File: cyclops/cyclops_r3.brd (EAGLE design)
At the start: 124.5 x 79.9 mm, 138 parts, among them Q1 BC817, Q2 IRF510, U1 MCP4921, U10 TLV2374, U11 THS4281, U12 MAX4564, U13 ZXTD, U14 ZXTD, U2 ADG3301, U3 MCP4022-50k, U4 LT1931, U5 LT1963A, U6 337L, U7 TLV3701, U8 ADR03, U9 OP1177, X1 SLP3, X2 SLP3, X3 SLP3

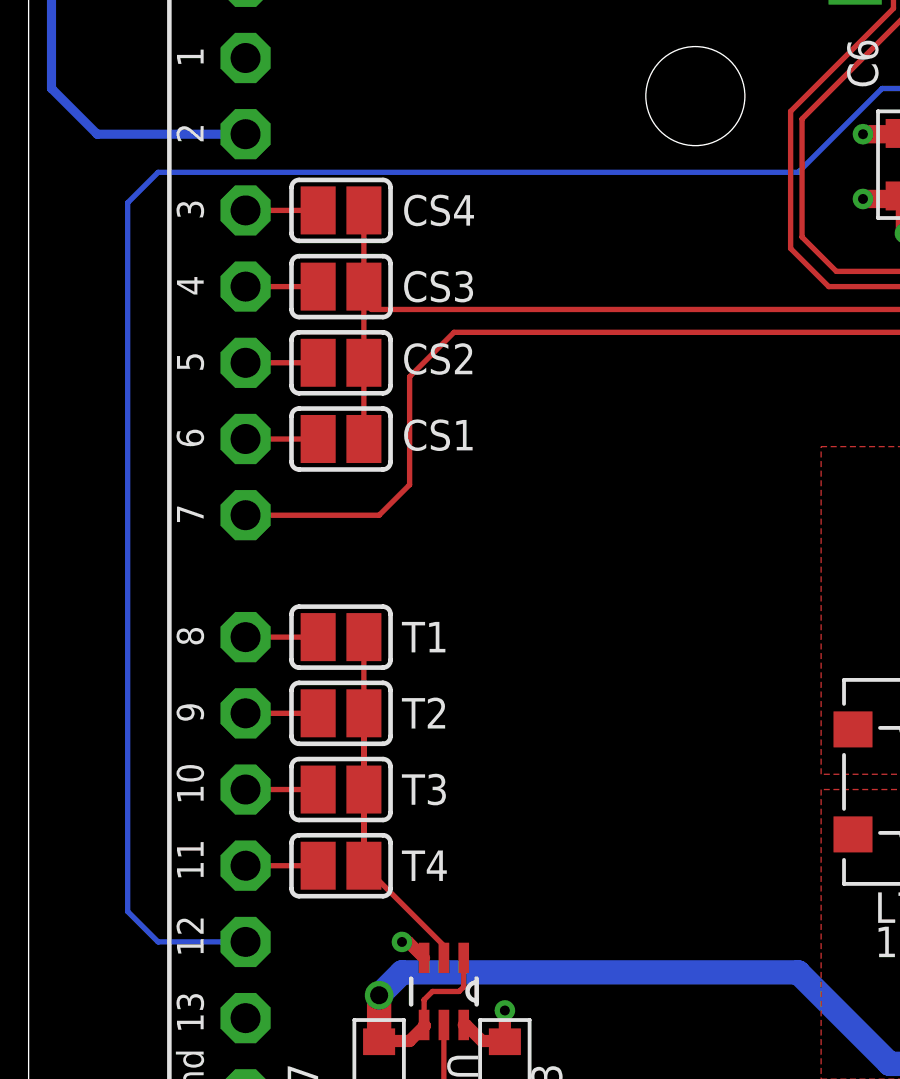
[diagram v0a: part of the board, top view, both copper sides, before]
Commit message: Refixed the incorrect labels on the jumper pads.
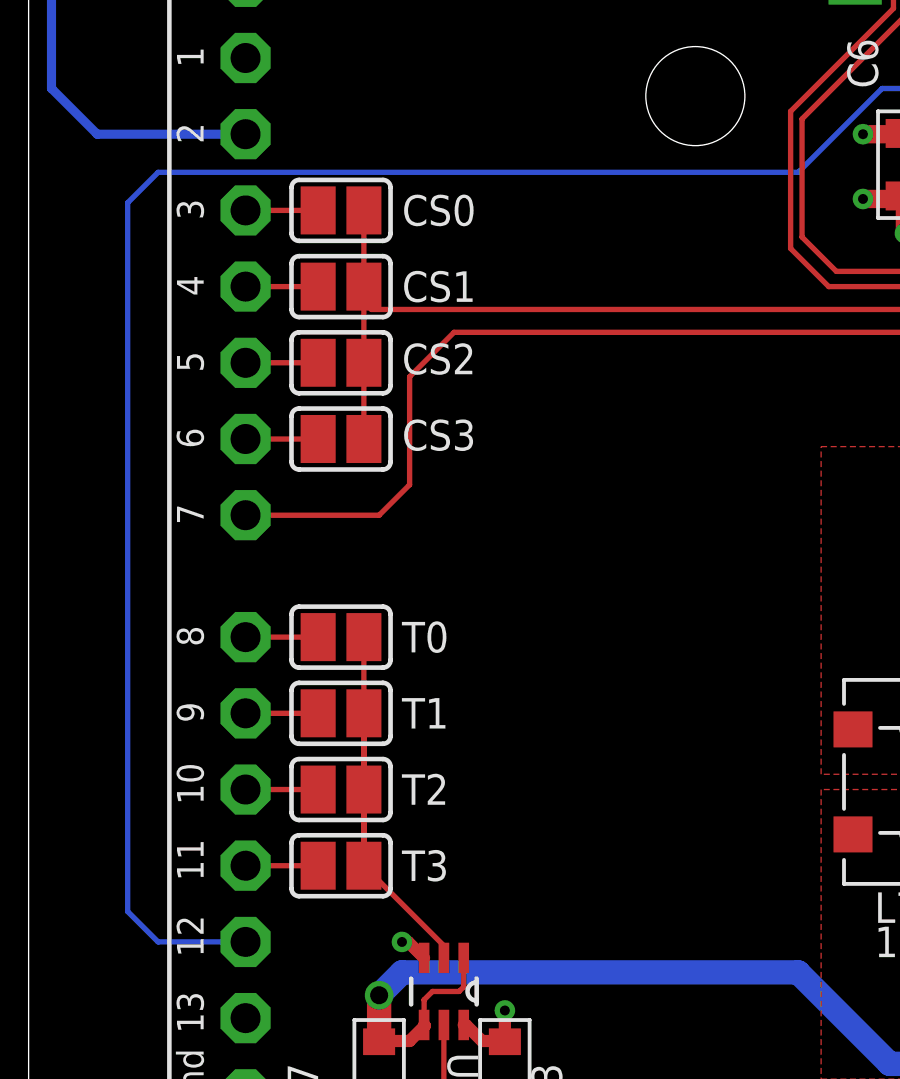
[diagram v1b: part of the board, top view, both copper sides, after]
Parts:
- removed T4: (no value), cyclops:SJ
- added T0: (no value), cyclops:SJ
- moved CS1 5.08 mm to (10.4, 53.3)
- moved CS3 5.08 mm to (10.4, 48.3)
- moved T1 2.54 mm to (10.4, 39.1)
- moved T2 2.54 mm to (10.4, 36.6)
- moved T3 2.54 mm to (10.4, 34.0)
- renumbered CS4 to CS0
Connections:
- net CS1: now also CS1.1; no longer CS3.1
- net CS3: now also CS3.1; no longer CS1.1
- net T0: now also T0.2; no longer T1.2
- net T1: now also T1.2; no longer T2.2
- net T2: now also T2.2; no longer T3.2
- net T3: now also T3.2; no longer T4.2
- net TRIG: now also T0.1; no longer T4.1
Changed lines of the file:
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@@
 <attribute name="VALUE" x="76.835" y="46.355" size="1.016" layer="27" font="vector" ratio="18" rot="R90" align="center-left"/>
 </element>
-<element name="CS1" library="cyclops" package="SJ" value="" x="10.414" y="48.26" smashed="yes">
+<element name="CS3" library="cyclops" package="SJ" value="" x="10.414" y="48.26" smashed="yes">
 <attribute name="NAME" x="12.446" y="47.879" size="1.016" layer="25" font="vector" ratio="18"/>
 <attribute name="VALUE" x="10.8141" y="48.26" size="0.02" layer="27"/>
@@
 <attribute name="VALUE" x="10.8141" y="50.8" size="0.02" layer="27"/>
 </element>
-<element name="CS3" library="cyclops" package="SJ" value="" x="10.414" y="53.34" smashed="yes">
+<element name="CS1" library="cyclops" package="SJ" value="" x="10.414" y="53.34" smashed="yes">
 <attribute name="NAME" x="12.446" y="52.832" size="1.016" layer="25" font="vector" ratio="18"/>
 <attribute name="VALUE" x="10.8141" y="53.34" size="0.02" layer="27"/>
 </element>
-<element name="CS4" library="cyclops" package="SJ" value="" x="10.414" y="55.88" smashed="yes">
+<element name="CS0" library="cyclops" package="SJ" value="" x="10.414" y="55.88" smashed="yes">
 <attribute name="NAME" x="12.446" y="55.372" size="1.016" layer="25" font="vector" ratio="18"/>
 <attribute name="VALUE" x="10.8141" y="55.88" size="0.02" layer="27"/>
@@
 <attribute name="VALUE" x="26.162" y="11.938" size="1.016" layer="27" font="vector" ratio="18" align="center-left"/>
 </element>
-<element name="T1" library="cyclops" package="SJ" value="" x="10.414" y="41.656" smashed="yes" rot="R180">
+<element name="T0" library="cyclops" package="SJ" value="" x="10.414" y="41.656" smashed="yes" rot="R180">
 <attribute name="NAME" x="12.446" y="41.148" size="1.016" layer="25" font="vector" ratio="18"/>
 <attribute name="VALUE" x="10.0139" y="41.656" size="0.02" layer="27" rot="R180"/>
 </element>
-<element name="T2" library="cyclops" package="SJ" value="" x="10.414" y="39.116" smashed="yes" rot="R180">
+<element name="T1" library="cyclops" package="SJ" value="" x="10.414" y="39.116" smashed="yes" rot="R180">
 <attribute name="NAME" x="12.446" y="38.608" size="1.016" layer="25" font="vector" ratio="18"/>
 <attribute name="VALUE" x="10.0139" y="39.116" size="0.02" layer="27" rot="R180"/>
 </element>
-<element name="T3" library="cyclops" package="SJ" value="" x="10.414" y="36.576" smashed="yes" rot="R180">
+<element name="T2" library="cyclops" package="SJ" value="" x="10.414" y="36.576" smashed="yes" rot="R180">
 <attribute name="NAME" x="12.446" y="36.068" size="1.016" layer="25" font="vector" ratio="18"/>
 <attribute name="VALUE" x="10.0139" y="36.576" size="0.02" layer="27" rot="R180"/>
 </element>
-<element name="T4" library="cyclops" package="SJ" value="" x="10.414" y="34.036" smashed="yes" rot="R180">
+<element name="T3" library="cyclops" package="SJ" value="" x="10.414" y="34.036" smashed="yes" rot="R180">
 <attribute name="NAME" x="12.446" y="33.528" size="1.016" layer="25" font="vector" ratio="18"/>
 <attribute name="VALUE" x="10.0139" y="34.036" size="0.02" layer="27" rot="R180"/>
@@
 </signal>
 <signal name="CS0">
-<contactref element="CS4" pad="1"/>
+<contactref element="CS0" pad="1"/>
 <contactref element="LEONARDO" pad="D3"/>
 <wire x1="9.652" y1="55.88" x2="7.232" y2="55.88" width="0.1778" layer="1"/>
 </signal>
 <signal name="CS1">
-<contactref element="CS3" pad="1"/>
+<contactref element="CS1" pad="1"/>
 <contactref element="LEONARDO" pad="D4"/>
 <wire x1="7.232" y1="53.34" x2="9.652" y2="53.34" width="0.1778" layer="1"/>
 </signal>
 <signal name="CS3">
-<contactref element="CS1" pad="1"/>
+<contactref element="CS3" pad="1"/>
 <contactref element="LEONARDO" pad="D6"/>
 <wire x1="7.232" y1="48.26" x2="9.652" y2="48.26" width="0.1778" layer="1"/>
@@
 <signal name="CS">
 <contactref element="U1" pad="2"/>
-<contactref element="CS4" pad="2"/>
+<contactref element="CS0" pad="2"/>
+<contactref element="CS1" pad="2"/>
+<contactref element="CS2" pad="2"/>
 <contactref element="CS3" pad="2"/>
-<contactref element="CS2" pad="2"/>
-<contactref element="CS1" pad="2"/>
 <wire x1="11.176" y1="55.88" x2="11.176" y2="53.34" width="0.1778" layer="1"/>
 <wire x1="11.176" y1="52.832" x2="11.176" y2="53.34" width="0.1778" layer="1"/>
@@
 </signal>
 <signal name="TRIG">
+<contactref element="T0" pad="1"/>
 <contactref element="T1" pad="1"/>
 <contactref element="T2" pad="1"/>
 <contactref element="T3" pad="1"/>
-<contactref element="T4" pad="1"/>
 <wire x1="11.176" y1="34.036" x2="11.176" y2="39.116" width="0.1778" layer="1"/>
 <wire x1="11.176" y1="39.116" x2="11.176" y2="36.576" width="0.1778" layer="1"/>
@@
 </signal>
 <signal name="T0">
-<contactref element="T1" pad="2"/>
+<contactref element="T0" pad="2"/>
 <contactref element="LEONARDO" pad="D8"/>
 <wire x1="9.652" y1="41.656" x2="7.232" y2="41.656" width="0.1778" layer="1"/>
 </signal>
 <signal name="T1">
-<contactref element="T2" pad="2"/>
+<contactref element="T1" pad="2"/>
 <contactref element="LEONARDO" pad="D9"/>
 <wire x1="7.232" y1="39.116" x2="9.652" y2="39.116" width="0.1778" layer="1"/>
 </signal>
 <signal name="T2">
-<contactref element="T3" pad="2"/>
+<contactref element="T2" pad="2"/>
 <contactref element="LEONARDO" pad="D10"/>
 <wire x1="9.652" y1="36.576" x2="7.232" y2="36.576" width="0.1778" layer="1"/>
 </signal>
 <signal name="T3">
-<contactref element="T4" pad="2"/>
+<contactref element="T3" pad="2"/>
 <contactref element="LEONARDO" pad="D11"/>
 <wire x1="7.232" y1="34.036" x2="9.652" y2="34.036" width="0.1778" layer="1"/>

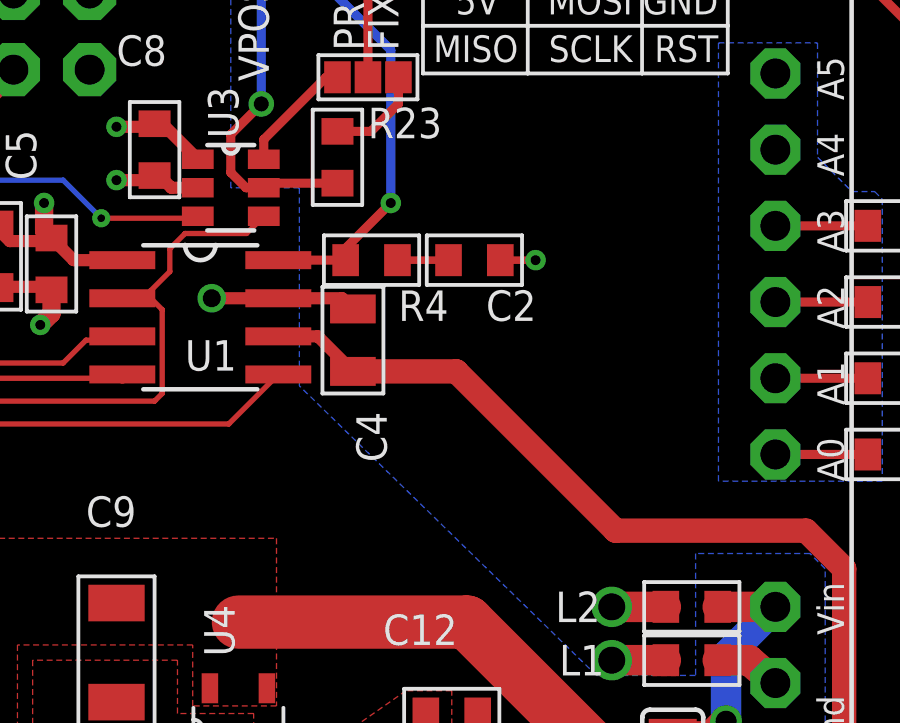
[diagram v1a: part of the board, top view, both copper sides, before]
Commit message: BOM simplification.
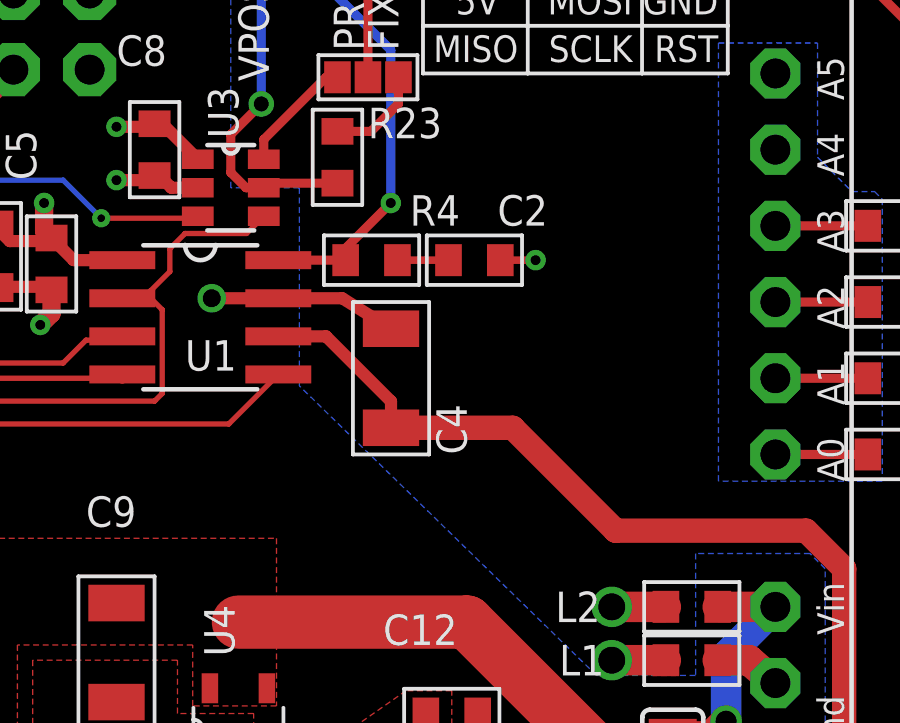
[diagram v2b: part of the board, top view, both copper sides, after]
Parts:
- C4: device cyclops:0805 -> cyclops:1206
- moved C4 1.80 mm to (42.7, 53.3)
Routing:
- net GND: track 116.4 -> 117.8 mm
- net REF2.5: track 65.9 -> 66.4 mm
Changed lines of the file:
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@@
 <attribute name="VALUE" x="33.401" y="51.435" size="1.016" layer="27" font="vector" ratio="18"/>
 </element>
-<element name="C4" library="cyclops" package="0805" value="10uF" x="41.409" y="54.61" smashed="yes" rot="R90">
-<attribute name="MN" value="TDK Corp." x="41.409" y="54.61" size="1.778" layer="27" rot="R90" display="off"/>
-<attribute name="PARTNO" value="C2012X5R1Cxxxxxxx" x="41.409" y="54.61" size="1.778" layer="27" rot="R90" display="off"/>
-<attribute name="DK" value="" x="41.409" y="54.61" size="1.778" layer="27" rot="R90" display="off"/>
-<attribute name="VID" value="DK" x="41.409" y="54.61" size="1.778" layer="27" rot="R90" display="off"/>
-<attribute name="NAME" x="42.538" y="50.546" size="1.016" layer="25" font="vector" ratio="18" rot="R90"/>
-<attribute name="VALUE" x="43.681" y="50.546" size="1.016" layer="27" font="vector" ratio="18" rot="R90"/>
+<element name="C4" library="cyclops" package="1206" value="10uF" x="42.679" y="53.34" smashed="yes" rot="R90">
+<attribute name="NAME" x="45.205" y="50.8" size="1.016" layer="25" font="vector" ratio="18" rot="R90"/>
+<attribute name="VALUE" x="46.602" y="50.8" size="1.016" layer="27" font="vector" ratio="18" rot="R90"/>
 </element>
 <element name="C5" library="cyclops" package="0603" value=".1uF" x="31.362" y="57.15" smashed="yes" rot="R270">
@@
 </element>
 <element name="C2" library="cyclops" package="0603" value="" x="45.459" y="57.277" smashed="yes">
-<attribute name="NAME" x="45.847" y="55.252" size="1.016" layer="25" font="vector" ratio="18"/>
+<attribute name="NAME" x="46.228" y="58.427" size="1.016" layer="25" font="vector" ratio="18"/>
 </element>
 <element name="R4" library="cyclops" package="0603" value="" x="42.03" y="57.277" smashed="yes" rot="R180">
@@
 <attribute name="DK" value="PxxxxHTR-ND" x="42.03" y="57.277" size="1.778" layer="27" rot="R180" display="off"/>
 <attribute name="MPN" value="ERJ-3EKFxxxxV" x="42.03" y="57.277" size="1.778" layer="27" rot="R180" display="off"/>
-<attribute name="NAME" x="42.926" y="55.252" size="1.016" layer="25" font="vector" ratio="18"/>
+<attribute name="NAME" x="43.307" y="58.427" size="1.016" layer="25" font="vector" ratio="18"/>
 </element>
 <element name="R29" library="cyclops" package="0603" value="0" x="78.225" y="38.735" smashed="yes" rot="R180">
@@
 <wire x1="64.636" y1="26.67" x2="64.636" y2="24.518" width="0.3048" layer="1"/>
 <wire x1="64.636" y1="24.518" x2="64.643" y2="24.511" width="0.3048" layer="1"/>
-<wire x1="41.409" y1="53.5686" x2="40.2406" y2="54.737" width="0.4064" layer="1"/>
-<wire x1="40.2406" y1="54.737" x2="38.922" y2="54.737" width="0.4064" layer="1"/>
-<wire x1="41.409" y1="53.5686" x2="44.8564" y2="53.5686" width="0.8128" layer="1"/>
-<wire x1="44.8564" y1="53.5686" x2="50.165" y2="48.26" width="0.8128" layer="1"/>
 <wire x1="50.165" y1="48.26" x2="56.515" y2="48.26" width="0.8128" layer="1"/>
 <wire x1="56.515" y1="48.26" x2="57.785" y2="46.99" width="0.8128" layer="1"/>
@@
 <wire x1="63.119" y1="24.511" x2="57.785" y2="29.845" width="0.8128" layer="16"/>
 <via x="57.785" y="35.687" extent="1-16" drill="0.8" diameter="0.3302"/>
+<wire x1="42.679" y1="51.689" x2="42.679" y2="52.571" width="0.4064" layer="1"/>
+<wire x1="42.679" y1="52.571" x2="40.513" y2="54.737" width="0.4064" layer="1"/>
+<wire x1="40.513" y1="54.737" x2="38.922" y2="54.737" width="0.4064" layer="1"/>
+<wire x1="50.165" y1="48.26" x2="46.736" y2="51.689" width="0.8128" layer="1"/>
+<wire x1="46.736" y1="51.689" x2="42.679" y2="51.689" width="0.8128" layer="1"/>
 </signal>
 <signal name="VAUX">
@@
 <wire x1="1.778" y1="79.248" x2="0.762" y2="78.232" width="0.3048" layer="2"/>
 <wire x1="0.762" y1="78.232" x2="0.762" y2="63.754" width="0.3048" layer="2"/>
-<wire x1="41.409" y1="55.6514" x2="41.0534" y2="56.007" width="0.4064" layer="1"/>
+<wire x1="42.679" y1="54.991" x2="41.0534" y2="56.007" width="0.4064" layer="1"/>
 <wire x1="41.0534" y1="56.007" x2="38.922" y2="56.007" width="0.4064" layer="1"/>
 <wire x1="29.21" y1="56.388" x2="31.496" y2="56.388" width="0.4064" layer="1"/>

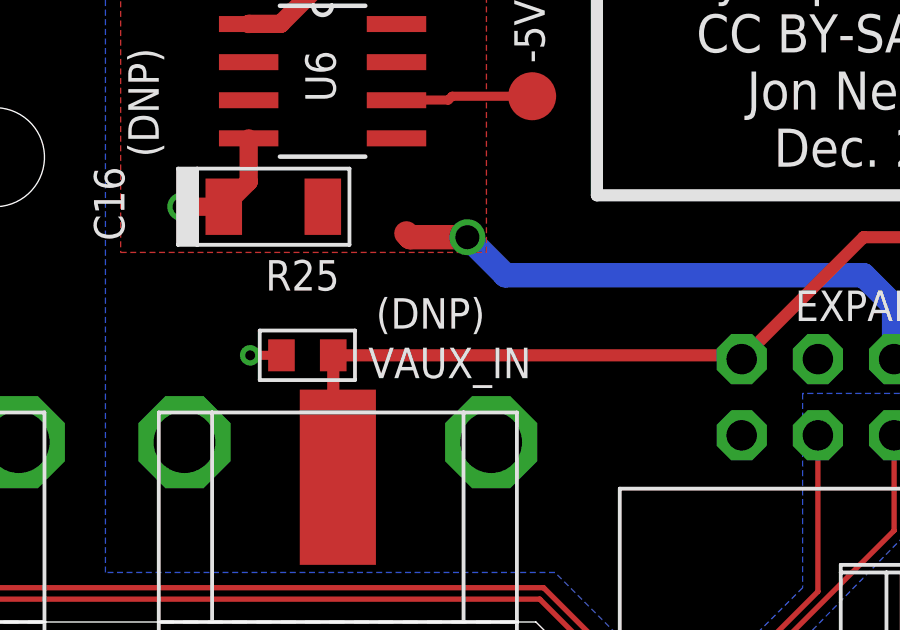
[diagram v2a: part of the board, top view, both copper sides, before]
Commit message: Replaced LT1963 with LT1764 to increase current capabilites.
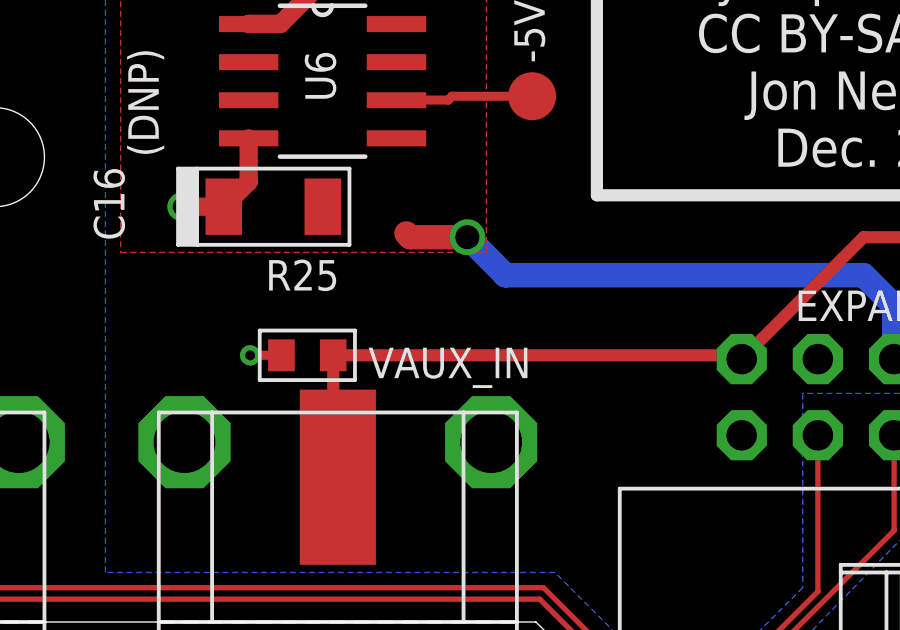
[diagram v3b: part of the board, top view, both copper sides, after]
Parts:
- U5: value LT1963A -> LT1764A
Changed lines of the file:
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@@
 SHORT IF NOT
 IN USE.</text>
-<text x="29.845" y="11.43" size="1.016" layer="21" font="vector" ratio="18">(DNP)</text>
 <text x="22.606" y="17.145" size="1.016" layer="21" font="vector" ratio="18" rot="R90">(DNP)</text>
 <text x="76.581" y="41.402" size="1.016" layer="21" font="vector" ratio="18">(DNP)</text>
@@
 </element>
 <element name="U$56" library="cyclops" package="CYCLOPS_LOGO" value="" x="38.01153125" y="38.350165625" rot="MR0"/>
-<element name="U5" library="cyclops" package="5-DDPAK" value="LT1963A" x="91.694" y="57.15" smashed="yes" rot="R90">
+<element name="U5" library="cyclops" package="5-DDPAK" value="LT1764A" x="91.694" y="57.15" smashed="yes" rot="R90">
 <attribute name="NAME" x="84.455" y="53.721" size="1.016" layer="25" font="vector" ratio="18" rot="R90"/>
 <attribute name="VALUE" x="85.725" y="53.721" size="1.016" layer="27" font="vector" ratio="18" rot="R90"/>
